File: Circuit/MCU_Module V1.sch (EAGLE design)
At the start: 29 parts, among them IC1 75176BD, J1 22-05-7048-04, Q1 8MHZ, T1 BC848, X1 PROG, X2 PWR&COM, X3 PWR&COM, X4 VIBRATION MOTOR

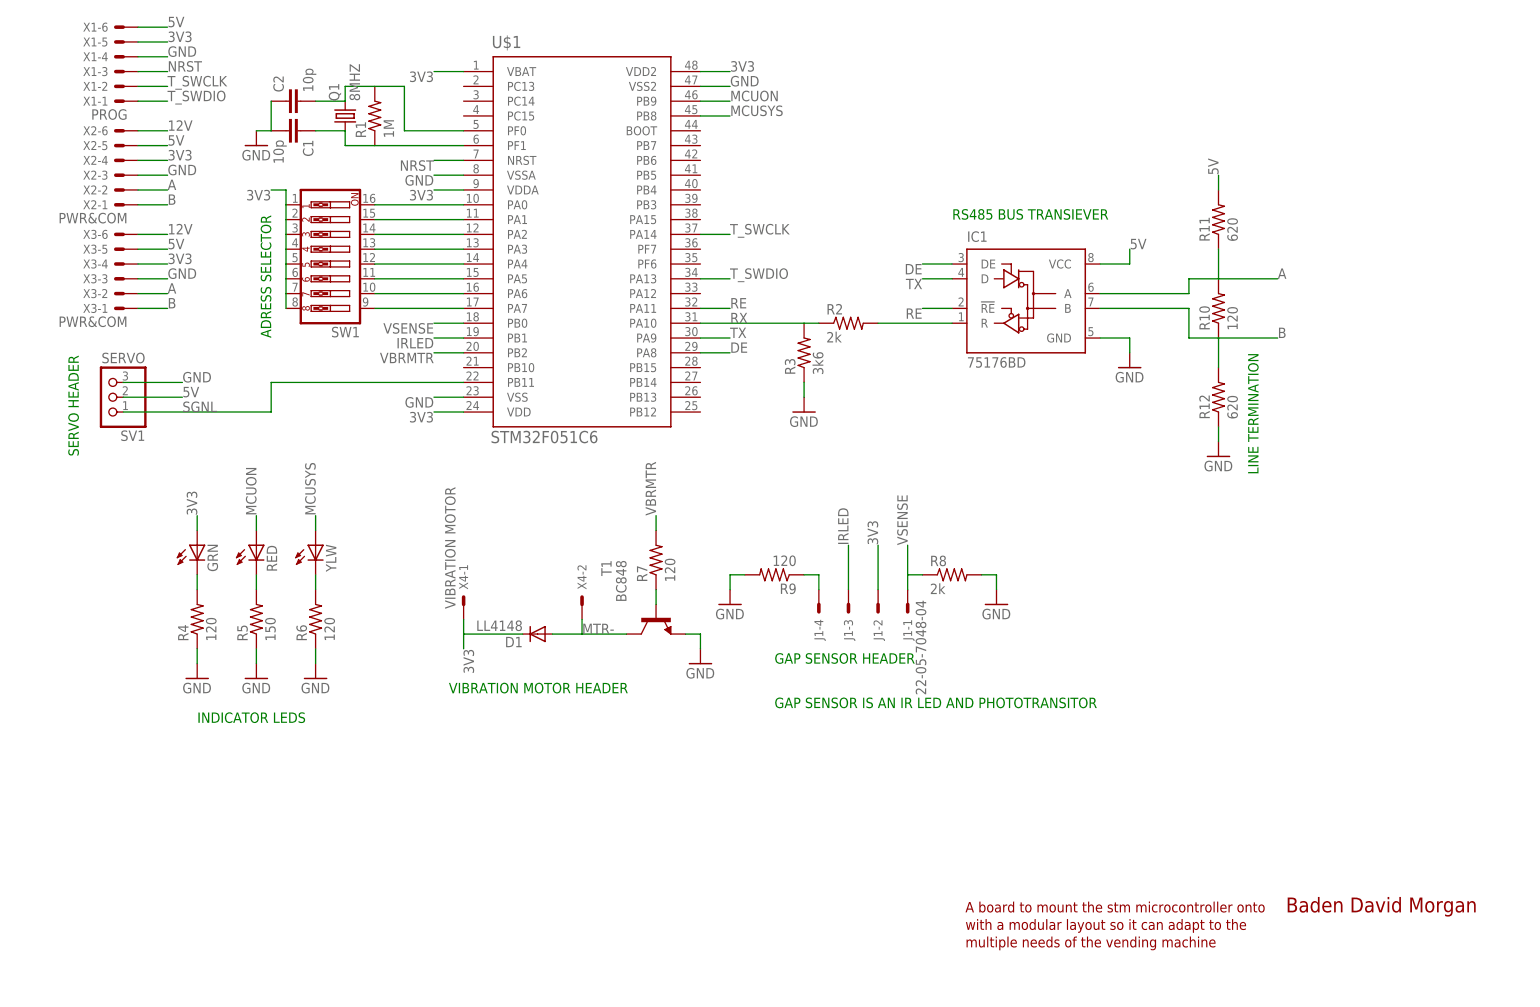
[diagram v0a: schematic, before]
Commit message: completed delivery idea 1 and progress on circuit
*finished first draft of delivery idea 1
*started delivery idea 2
*made progress on circuit
*finished schematic
*half way through layout
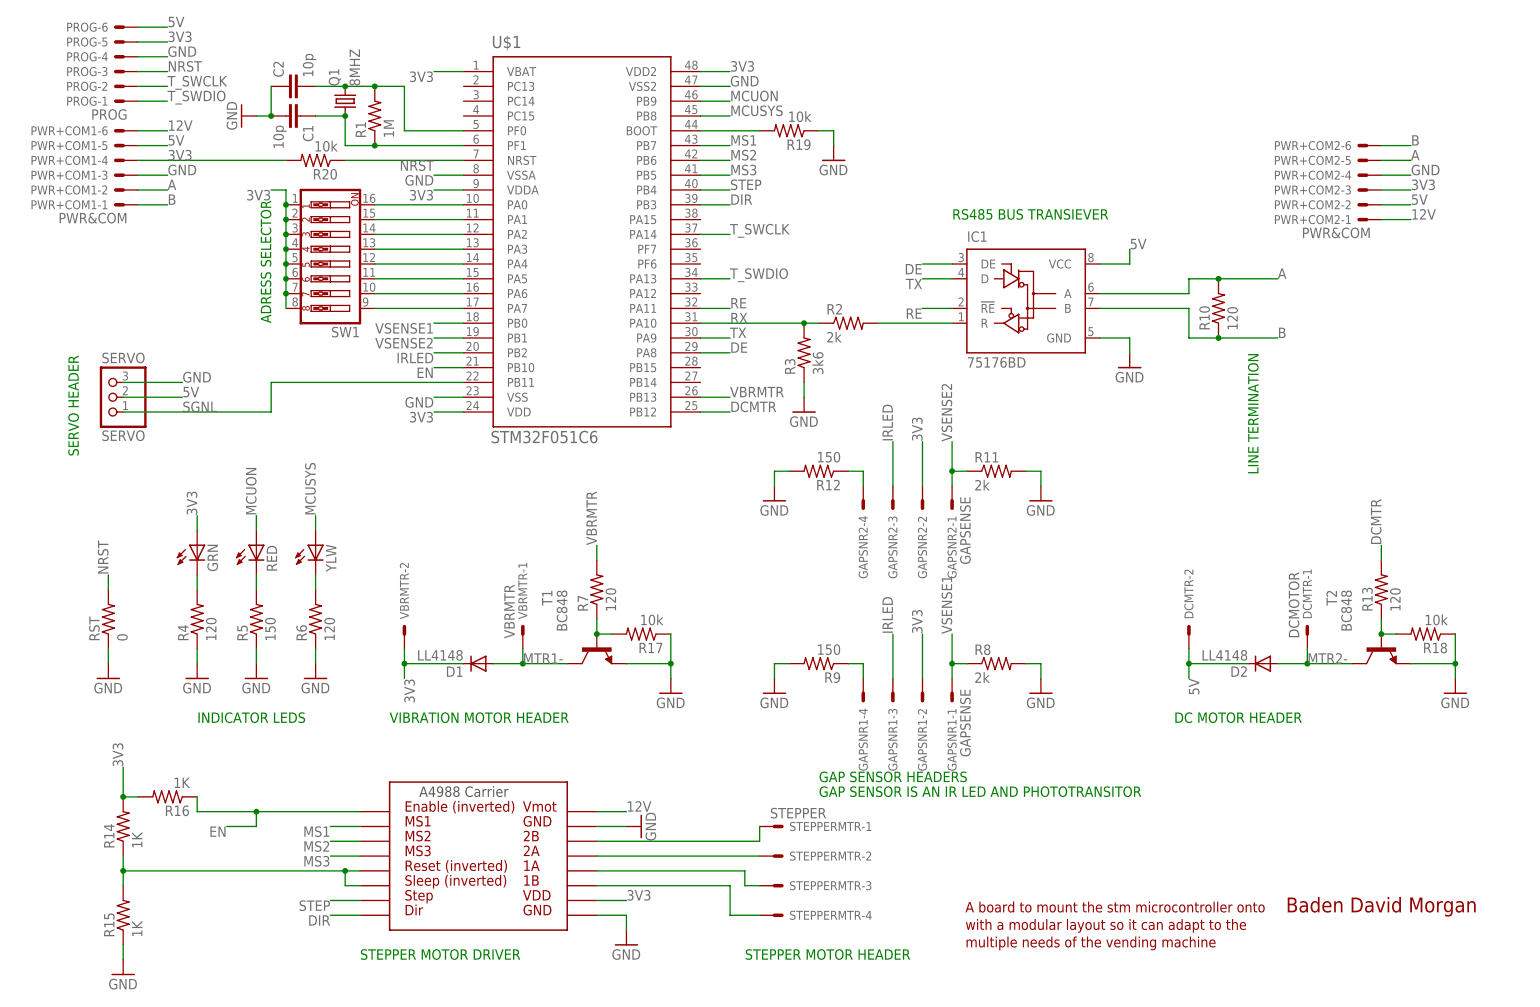
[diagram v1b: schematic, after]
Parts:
- removed J1: 22-05-7048-04, con-molex:22-05-7048-04
- removed SV1: SERVO, pinhead:PINHD-1X3/90
- removed X1: PROG, con-molex:22-05-7068-06
- removed X3: PWR&COM, con-molex:22-05-7068-06
- removed X4: VIBRATION MOTOR, con-molex:22-23-2021
- added D2: LL4148, diode:PMLL4150
- added DCMTR: DCMOTOR, con-molex:22-27-2021-02
- added GAPSNR1, GAPSNR2: GAPSENSE, con-molex:22-27-2041-04
- added PROG: PROG, con-molex:22-27-2061-06
- added PWR+COM2: PWR&COM, con-molex:22-05-7068-06
- added R13: 120, rcl:R-US_R0805
- added R14, R15, R16: 1K, rcl:R-US_R0805
- added R17, R18, R19, R20: 10k, rcl:R-US_R0805
- added RST: 0, rcl:R-US_R0805
- added SERVO: SERVO, pinhead:PINHD-1X3
- added STEPPERMTR: STEPPER, con-molex:22-27-2041-04
- added T2: BC848, transistor:BC848
- added U$2: A4983CARRIER, RepRapjr:A4983CARRIER
- added VBRMTR: VBRMTR, con-molex:22-27-2021-02
- R11: value 620 -> 2k
- R12: value 620 -> 150; device resistor:R-US_R0805 -> rcl:R-US_R0805
- R9: value 120 -> 150
- renumbered X2 to PWR+COM1
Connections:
- removed net MTR-: D1.A, T1.C, X4-2.S
- removed net VSENSE: J1-1.S, R8.1, U$1.PB0
- new net DCMTR: R13.2, U$1.PB12
- new net DIR: U$1.PB3, U$2.DIR
- new net EN: R16.1, U$1.PB10, U$2.EN
- new net MS1: U$1.PB7, U$2.MS1
- new net MS2: U$1.PB6, U$2.MS2
- new net MS3: U$1.PB5, U$2.MS3
- new net MTR1-: D1.A, T1.C, VBRMTR-1.S
- new net MTR2-: D2.A, DCMTR-1.S, T2.C
- new net N$18: STEPPERMTR-3.S, U$2.1A
- new net N$20: STEPPERMTR-2.S, U$2.2A
- new net N$21: STEPPERMTR-1.S, U$2.2B
- new net N$22: R19.2, U$1.BOOT
- new net N$24: GAPSNR2-4.S, R12.1
- new net N$26: R14.1, R15.2, U$2.RST, U$2.SLEEP
- new net N$4: R13.1, R18.2, T2.B
- new net N$5: STEPPERMTR-4.S, U$2.1B
- new net STEP: U$1.PB4, U$2.STEP
- new net VSENSE1: GAPSNR1-1.S, R8.1, U$1.PB0
- new net VSENSE2: GAPSNR2-1.S, R11.1, U$1.PB1
- net 12V: now also PWR+COM2-1.S, U$2.VMOT; no longer X3-6.S
- net 3V3: now also GAPSNR1-2.S, GAPSNR2-2.S, PROG-5.S, PWR+COM2-3.S, R14.2, R16.2, R20.2, U$2.VDD, VBRMTR-2.S; no longer J1-2.S, X1-5.S, X3-4.S, X4-1.S
- net 5V: now also D2.C, DCMTR-2.S, PROG-6.S, PWR+COM2-2.S, SERVO.2; no longer R11.2, SV1.2, X1-6.S, X3-5.S
- net A: now also PWR+COM2-5.S; no longer R11.1, X3-2.S
- net B: now also PWR+COM2-6.S; no longer R12.2, X3-1.S
- net GND: now also PROG-4.S, PWR+COM2-4.S, R11.2, R12.2, R15.1, R17.1, R18.1, R19.1, RST.1, SERVO.3, T2.E, U$2.GND@0, U$2.GND@1; no longer R12.1, SV1.3, X1-4.S, X3-3.S
- net IRLED: now also GAPSNR1-3.S, GAPSNR2-3.S, U$1.PB2; no longer J1-3.S, U$1.PB1
- net N$17: now also R17.2
- net N$19: now also GAPSNR1-4.S; no longer J1-4.S
- net NRST: now also PROG-3.S, R20.1, RST.2; no longer X1-3.S
- net SGNL: now also SERVO.1; no longer SV1.1
- net T_SWCLK: now also PROG-2.S; no longer X1-2.S
- net T_SWDIO: now also PROG-1.S; no longer X1-1.S
- net VBRMTR: now also U$1.PB13; no longer U$1.PB2
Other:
- note added: "DC MOTOR HEADER"
- note added: "GAP SENSOR HEADERS"
- note added: "STEPPER MOTOR DRIVER"
- note added: "STEPPER MOTOR HEADER"
- note removed: "GAP SENSOR HEADER"
- moved on the sheet: C1, C2, D1, Q1, R11, R12, R7, R8, R9, T1
